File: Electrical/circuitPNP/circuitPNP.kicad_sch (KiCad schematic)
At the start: 8 parts, among them Q1 GS66504B, Q2 GS66504B, U1 ESP32-S3-WROOM-1, U2 STMPE1600

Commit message: wip and gitignore update
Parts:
- removed U2: STMPE1600, Package_DFN_QFN:QFN-24-1EP_4x4mm_P0.5mm_EP2.6x2.6mm, symbol Interface_Expansion:STMPE1600
- added C1, C13, C17, C8, C9: 0.1uf, Capacitor_SMD:C_0603_1608Metric_Pad1.08x0.95mm_HandSolder, symbol Device:C
- added C12, C16, C2: 10uf, Capacitor_SMD:C_0603_1608Metric_Pad1.08x0.95mm_HandSolder, symbol Device:C
- added C7: 1uf/16V 10%, Capacitor_SMD:C_0603_1608Metric_Pad1.08x0.95mm_HandSolder, symbol Device:C
- added D3: SP0503BAHT, Package_TO_SOT_SMD:SOT-143, symbol Power_Protection:SP0503BAHT
- added D7: NUP2105L, Package_TO_SOT_SMD:SOT-23, symbol Power_Protection:NUP2105L
- added J1: USB_C_Receptacle_USB2.0_16P, Connector_USB:USB_C_Receptacle_GCT_USB4105-xx-A_16P_TopMnt_Horizontal, symbol Connector:USB_C_Receptacle_USB2.0_16P
- added J4: Conn_01x02_Pin, Connector_PinHeader_2.54mm:PinHeader_1x02_P2.54mm_Vertical, symbol Connector:Conn_01x02_Pin
- added J6: Conn_01x02_Pin, Connector_Molex:Molex_KK-396_A-41792-0002_1x02_P3.96mm_Horizontal, symbol Connector:Conn_01x02_Pin
- added R1, R2, R3, R4: 22, Resistor_SMD:R_0603_1608Metric_Pad0.98x0.95mm_HandSolder, symbol Device:R
- added R10: 10k 1%, Resistor_SMD:R_0603_1608Metric_Pad0.98x0.95mm_HandSolder, symbol Device:R
- added R12: 120, Resistor_SMD:R_0603_1608Metric_Pad0.98x0.95mm_HandSolder, symbol Device:R
- added R5, R6: 5.1k, Resistor_SMD:R_0603_1608Metric_Pad0.98x0.95mm_HandSolder, symbol Device:R
- added R7: 1, Resistor_SMD:R_0603_1608Metric_Pad0.98x0.95mm_HandSolder, symbol Device:R
- added SW1, SW2: SW_Push, Button_Switch_SMD:SW_SPST_PTS647_Sx38, symbol Switch:SW_Push
- added U3: SN65HVD230, Package_SO:SOIC-8_3.9x4.9mm_P1.27mm, symbol Interface_CAN_LIN:SN65HVD230
- added U4: AMS1117-3.3, Package_TO_SOT_SMD:SOT-223-3_TabPin2, symbol Regulator_Linear:AMS1117-3.3
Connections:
- net GND: now reaches U1.1 (GND), U1.40 (GND), U1.41 (GND)
- net GND: now also C1.1, C12.1, C13.2, C16.1, C17.1, C2.1, C7.2, C8.1, C9.2, D3.1 (A), D7.3 (A), J1.A1 (GND), J1.A12 (GND), J1.B1 (GND), J1.B12 (GND), R5.2, R6.2, R7.2, SW1.1, SW2.1, U3.2 (GND), U3.8 (Rs), U4.1 (GND)
- net GPIO17: now reaches U1.10 (IO17)
- net GPIO18: now reaches U1.11 (IO18)
- net GPIO8: now reaches U1.12 (IO8)
- net D-: now reaches U1.13 (USB_D-)
- net D-: now also D3.2 (K), R3.2, R4.2
- net D+: now reaches U1.14 (USB_D+)
- net D+: now also D3.3 (K), R1.2, R2.2
- net GPIO3: now reaches U1.15 (IO3)
- net GPIO3: now also U3.4 (R)
- net GPIO46: now reaches U1.16 (IO46)
- net GPIO9: now reaches U1.17 (IO9)
- net GPIO10: now reaches U1.18 (IO10)
- net GPIO11: now reaches U1.19 (IO11)
- net 3V3: now reaches U1.2 (3V3)
- net 3V3: now also C12.2, C8.2, R10.1, U3.3 (VCC)
- net GPIO12: now reaches U1.20 (IO12)
- net GPIO13: now reaches U1.21 (IO13)
- net GPIO14: now reaches U1.22 (IO14)
- net GPIO21: now reaches U1.23 (IO21)
- net GPIO47: now reaches U1.24 (IO47)
- net GPIO48: now reaches U1.25 (IO48)
- net GPIO45: now reaches U1.26 (IO45)
- net GPIO0: now reaches U1.27 (IO0)
- net GPIO0: now also C9.1, SW1.2
- net GPIO35: now reaches U1.28 (IO35)
- net GPIO36: now reaches U1.29 (IO36)
- net CHIP_PU: now reaches U1.3 (EN)
- net CHIP_PU: now also C13.1, C7.1, R10.2, SW2.2
- net GPIO37: now reaches U1.30 (IO37)
- net GPIO38: now reaches U1.31 (IO38)
- net GPIO39: now reaches U1.32 (IO39)
- net GPIO40: now reaches U1.33 (IO40)
- net GPIO41: now reaches U1.34 (IO41)
- net GPIO42: now reaches U1.35 (IO42)
- net RX: now reaches U1.36 (RXD0)
- net RX: now also J4.2 (Pin_2)
- net TX: now reaches U1.37 (TXD0)
- net TX: now also J4.1 (Pin_1)
- net GPIO2: now reaches U1.38 (IO2)
- net GPIO1: now reaches U1.39 (IO1)
- net GPIO1: now also U3.1 (D)
- net GPIO4: now reaches U1.4 (IO4)
- net GPIO5: now reaches U1.5 (IO5)
- net GPIO6: now reaches U1.6 (IO6)
- net GPIO7: now reaches U1.7 (IO7)
- net GPIO15: now reaches U1.8 (IO15)
- net GPIO16: now reaches U1.9 (IO16)
- new net: J1.S1 (SHIELD), R7.1
- new net: J1.B5 (CC2), R6.1
- new net: J1.B6 (D+), R1.1
- new net: J1.B7 (D-), R3.1
- new net: J1.A7 (D-), R4.1
- new net: J1.A5 (CC1), R5.1
- new net: J1.A6 (D+), R2.1
- new net 3V3_5: C16.2, C17.2, U4.2 (VO)
- new net CANH: D7.1 (K), J6.1 (Pin_1), R12.2, U3.7 (CANH)
- new net CANL: D7.2 (K), J6.2 (Pin_2), R12.1, U3.6 (CANL)
- new net VBus: C1.2, C2.2, D3.4 (K), J1.A4 (VBUS), J1.A9 (VBUS), J1.B4 (VBUS), J1.B9 (VBUS), U4.3 (VI)
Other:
- note added: "Circuit Can"
- note added: "Circuit ESP32"
- note added: "Circuit USB type c"
- moved on the sheet: A1, A2, A3, A4, Q1, Q2

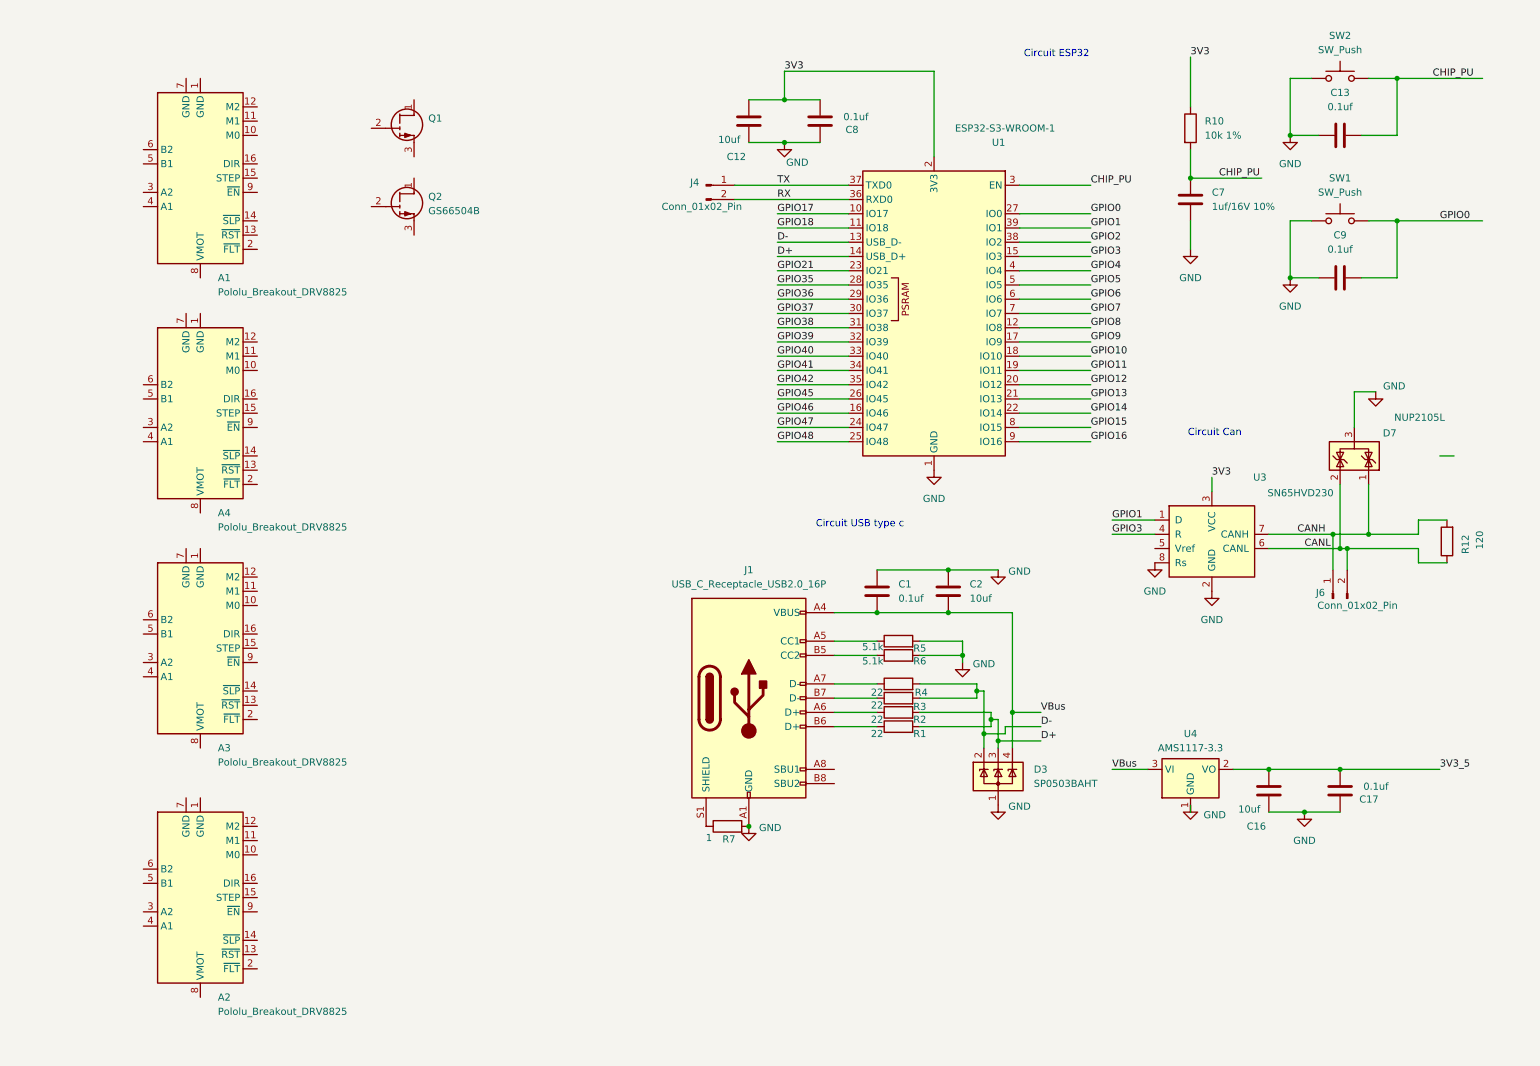
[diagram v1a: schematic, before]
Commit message: wip, most part are on the circuit, mssing connection
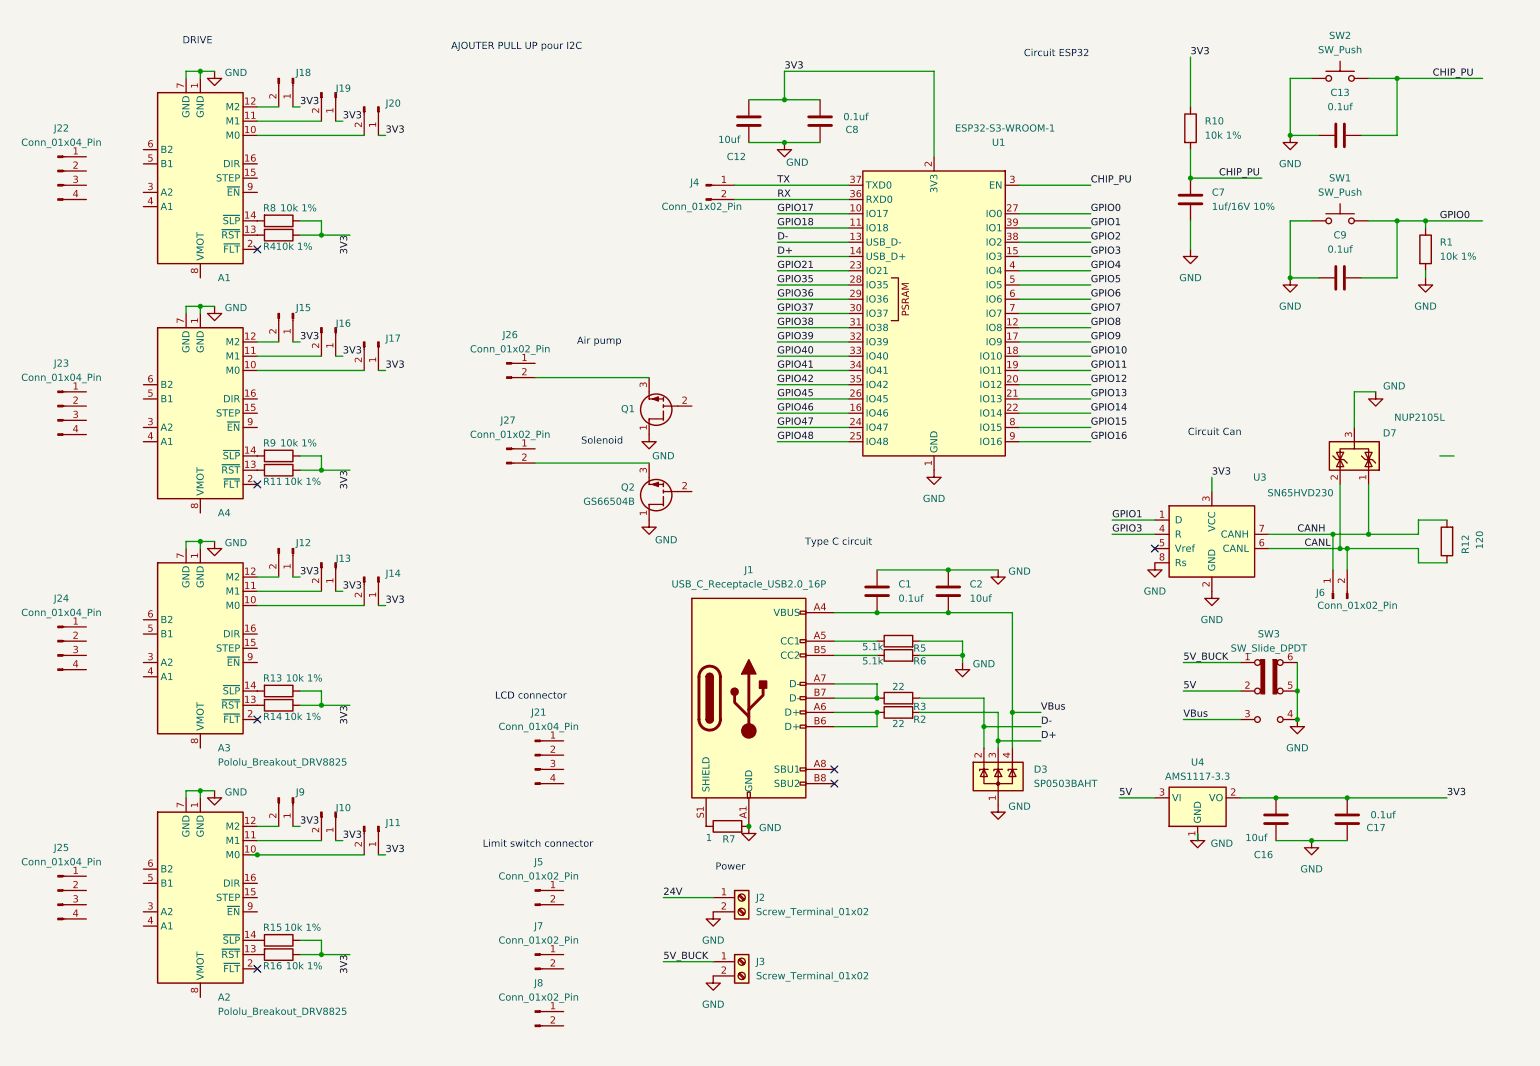
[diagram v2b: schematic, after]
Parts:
- added J10, J11, J12, J13, J14, J15, J16, J17, J18, J19, J20, J26, J27, J5, J7, J8, J9: Conn_01x02_Pin, symbol Connector:Conn_01x02_Pin
- added J2, J3: Screw_Terminal_01x02, symbol Connector:Screw_Terminal_01x02
- added J21, J22, J23, J24, J25: Conn_01x04_Pin, symbol Connector:Conn_01x04_Pin
- added R11, R13, R14, R15, R16, R8, R9: 10k 1%, Resistor_SMD:R_0603_1608Metric_Pad0.98x0.95mm_HandSolder, symbol Device:R
- added SW3: SW_Slide_DPDT, symbol Switch:SW_Slide_DPDT
- R1, R4: value 22 -> 10k 1%
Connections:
- net 3V3_5 is gone; now on net 3V3: C16.2, C17.2, U4.2 (VO)
- net 3V3: now also R4.1, J10.1 (Pin_1), J11.1 (Pin_1), J12.1 (Pin_1), J13.1 (Pin_1), J14.1 (Pin_1), J15.1 (Pin_1), J16.1 (Pin_1), J17.1 (Pin_1), J18.1 (Pin_1), J19.1 (Pin_1), J20.1 (Pin_1), J9.1 (Pin_1), R11.1, R13.1, R14.1, R15.1, R16.1, R8.1, R9.1
- net D+: no longer R1.2
- net D-: no longer R4.2
- net GND: now also A1.1 (GND), A1.7 (GND), A2.1 (GND), A2.7 (GND), A3.1 (GND), A3.7 (GND), A4.1 (GND), A4.7 (GND), Q1.1 (D), Q2.1 (D), R1.2, J2.2 (Pin_2), J3.2 (Pin_2), SW3.4 (A), SW3.5 (B), SW3.6 (C)
- net GPIO0: now also R1.1
- net VBus: now also SW3.3 (C); no longer U4.3 (VI)
- net at A1.10 (M0): now also J20.2 (Pin_2)
- net at A1.11 (M1): now also J19.2 (Pin_2)
- net at A1.12 (M2): now also J18.2 (Pin_2)
- net at A1.13 (~{RST}): now also R4.2
- net at A1.14 (~{SLP}): now also R8.2
- net at A4.10 (M0): now also J17.2 (Pin_2)
- net at A4.11 (M1): now also J16.2 (Pin_2)
- net at A4.12 (M2): now also J15.2 (Pin_2)
- net at A4.13 (~{RST}): now also R11.2
- net at A4.14 (~{SLP}): now also R9.2
- net at J1.B6 (D+): now also J1.A6 (D+), R2.1; no longer R1.1
- net at A3.10 (M0): now also J14.2 (Pin_2)
- net at A3.11 (M1): now also J13.2 (Pin_2)
- net at A3.12 (M2): now also J12.2 (Pin_2)
- net at A3.13 (~{RST}): now also R14.2
- net at A3.14 (~{SLP}): now also R13.2
- net at J1.B7 (D-), R3.1: now also J1.A7 (D-)
- net at A2.10 (M0): now also J11.2 (Pin_2)
- net at A2.11 (M1): now also J10.2 (Pin_2)
- net at A2.12 (M2): now also J9.2 (Pin_2)
- net at A2.13 (~{RST}): now also R16.2
- net at A2.14 (~{SLP}): now also R15.2
- net at Q2.3 (S): now also J27.2 (Pin_2)
- net at Q1.3 (S): now also J26.2 (Pin_2)
- new net 24V: J2.1 (Pin_1)
- new net 5V: SW3.2 (B), U4.3 (VI)
- new net 5V_BUCK: J3.1 (Pin_1), SW3.1 (A)
- no-connect marks 0 -> 7
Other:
- note added: "AJOUTER PULL UP pour I2C"
- note added: "Air pump"
- note added: "DRIVE"
- note added: "LCD connector"
- note added: "Limit switch connector"
- note added: "Power"
- note added: "Solenoid"
- note added: "Type C circuit"
- note removed: "Circuit USB type c"
- moved on the sheet: C16, C17, Q1, Q2, U4

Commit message: gitignore update and circuit mostly done, only missing bulck cap value
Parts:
- added C10, C14, C18, C21, C3, C5: 0.1uF, symbol Device:C
- added C11, C15, C19, C20, C4, C6: 100uF?, symbol Device:C
- added D1: D_TVS, symbol Device:D_TVS
- added J28: Conn_01x04_Pin, symbol Connector:Conn_01x04_Pin
- added R17, R18: 4.7k, Resistor_SMD:R_0603_1608Metric_Pad0.98x0.95mm_HandSolder, symbol Device:R
- added R19, R20, R21: 10k, Resistor_SMD:R_0603_1608Metric_Pad0.98x0.95mm_HandSolder, symbol Device:R
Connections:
- net GPIO8 is gone; now on net SDA: U1.12 (IO8)
- net GPIO9 is gone; now on net SCL: U1.17 (IO9)
- net 24V: now also A1.8 (VMOT), A2.8 (VMOT), A3.8 (VMOT), A4.8 (VMOT), C10.1, C11.1, C14.1, C15.1, C20.1, C21.1, C3.1, C4.1, C5.1, C6.1, D1.2 (A2)
- net 3V3: now also J21.2 (Pin_2), J28.1 (Pin_1), R17.2, R18.2, R19.1, R20.1, R21.1
- net 5V: now also J26.1 (Pin_1), J27.1 (Pin_1)
- net 5V_BUCK: now also C18.1, C19.1
- net GND: now also J21.1 (Pin_1), J5.2 (Pin_2), J7.2 (Pin_2), J8.2 (Pin_2), C10.2, C11.2, C14.2, C15.2, C18.2, C19.2, C20.2, C21.2, C3.2, C4.2, C5.2, C6.2, D1.1 (A1), J28.4 (Pin_4)
- net GPIO1: now also J28.2 (Pin_2); no longer U3.1 (D)
- net GPIO10: now also A3.9 (~{EN})
- net GPIO11: now also A2.16 (DIR)
- net GPIO12: now also A2.15 (STEP)
- net GPIO13: now also A2.9 (~{EN}), Q1.2 (G)
- net GPIO15: now also A4.15 (STEP)
- net GPIO16: now also A4.9 (~{EN})
- net GPIO17: now also A3.16 (DIR)
- net GPIO18: now also A3.15 (STEP)
- net GPIO2: now also J28.3 (Pin_3)
- net GPIO21: now also Q2.2 (G)
- net GPIO3: no longer U3.4 (R)
- net GPIO35: now also J5.1 (Pin_1), R19.2
- net GPIO36: now also J7.1 (Pin_1), R20.2
- net GPIO37: now also J8.1 (Pin_1), R21.2
- net GPIO4: now also A1.16 (DIR)
- net GPIO47: now also U3.4 (R)
- net GPIO48: now also U3.1 (D)
- net GPIO5: now also A1.15 (STEP)
- net GPIO6: now also A1.9 (~{EN})
- net GPIO7: now also A4.16 (DIR)
- net at J23.1 (Pin_1): now also A4.6 (B2)
- net at J23.2 (Pin_2): now also A4.5 (B1)
- net at J23.3 (Pin_3): now also A4.3 (A2)
- net at J23.4 (Pin_4): now also A4.4 (A1)
- net at A1.3 (A2): now also J22.3 (Pin_3)
- net at A1.4 (A1): now also J22.4 (Pin_4)
- net at A1.5 (B1): now also J22.2 (Pin_2)
- net at A1.6 (B2): now also J22.1 (Pin_1)
- net at A3.3 (A2): now also J24.3 (Pin_3)
- net at A3.4 (A1): now also J24.4 (Pin_4)
- net at A3.5 (B1): now also J24.2 (Pin_2)
- net at A3.6 (B2): now also J24.1 (Pin_1)
- net at A2.3 (A2): now also J25.3 (Pin_3)
- net at A2.4 (A1): now also J25.4 (Pin_4)
- net at A2.5 (B1): now also J25.2 (Pin_2)
- net at A2.6 (B2): now also J25.1 (Pin_1)
- net SDA: now reaches J21.3 (Pin_3)
- net SDA: now also R17.1
- net SCL: now reaches J21.4 (Pin_4)
- net SCL: now also R18.1
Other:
- note added: "Capteur de pression"
- note removed: "AJOUTER PULL UP pour I2C"
- moved on the sheet: A1, A4, J15, J16, J17, J18, J19, J2, J20, J21, J22, J3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
